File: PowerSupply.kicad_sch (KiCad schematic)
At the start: 0 parts

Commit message: i have added a few resistores
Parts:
- added C1: CL10A475KO8NNNC, easyeda2kicad:C0603, symbol easyeda2kicad:CL10A475KO8NNNC
- added R1: 0603WAF1003T5E, easyeda2kicad:R0603, symbol easyeda2kicad:0603WAF1003T5E
- added U1: TPS55288RPMR, easyeda2kicad:VQFN-HR-26_L4.0-W3.5_TPS55288RPMR, symbol easyeda2kicad:TPS55288RPMR
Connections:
- new net: C1.1, U1.19 (VCC)
- new net GND: C1.2

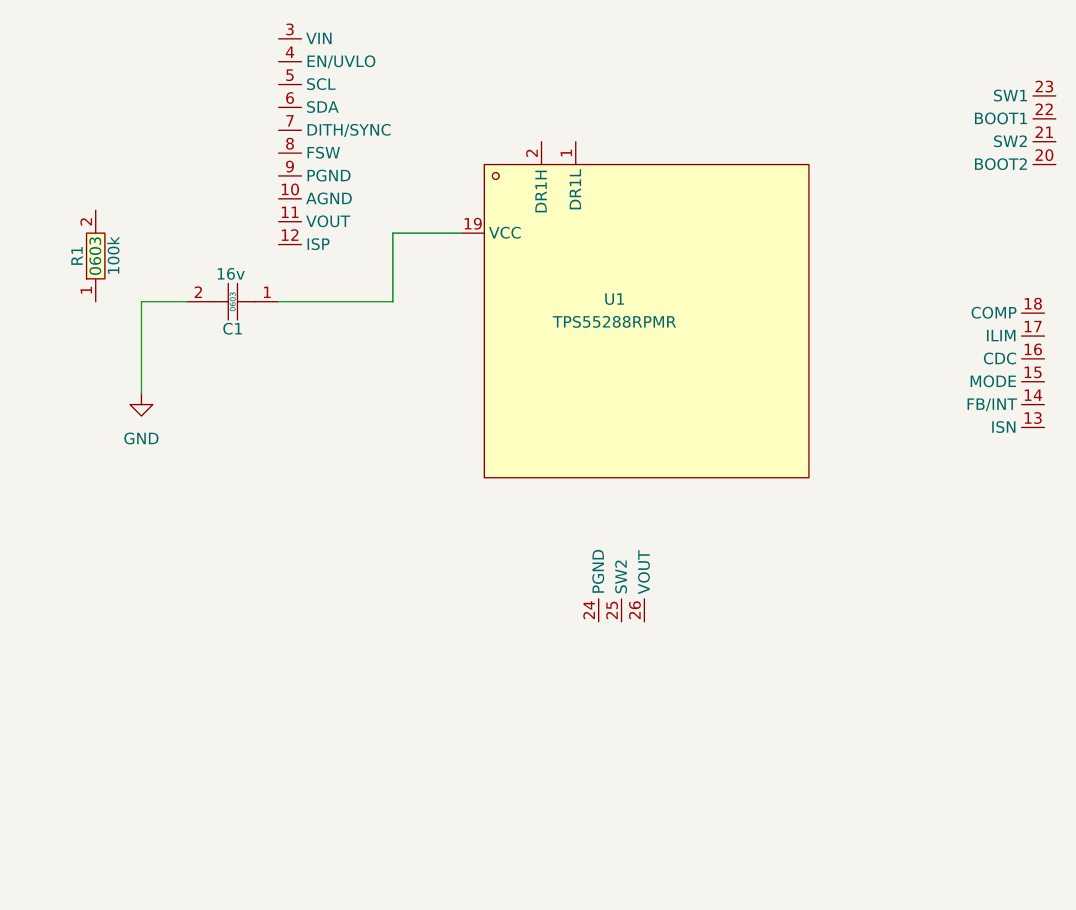
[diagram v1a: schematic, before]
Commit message: Added a few cap + res+ transistors
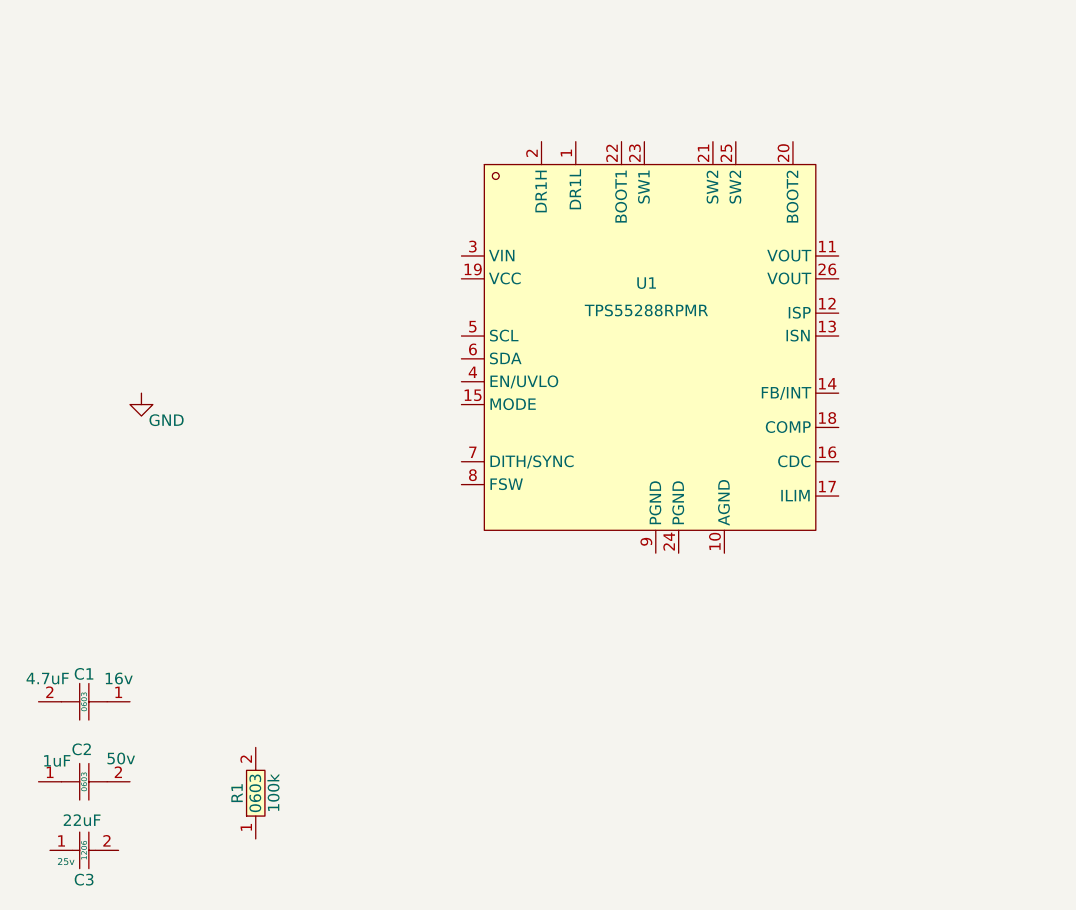
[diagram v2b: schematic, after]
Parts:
- added C2: CL10A105KB8NNNC, easyeda2kicad:C0603, symbol easyeda2kicad:CL10A105KB8NNNC
- added C3: CL31A226KAHNNNE, easyeda2kicad:C1206, symbol easyeda2kicad:CL31A226KAHNNNE
- C1: Field8 (none) -> 4.7uF
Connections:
- net GND: no longer C1.2
- net at C1.1: no longer U1.19 (VCC)
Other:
- moved on the sheet: C1, R1, U1

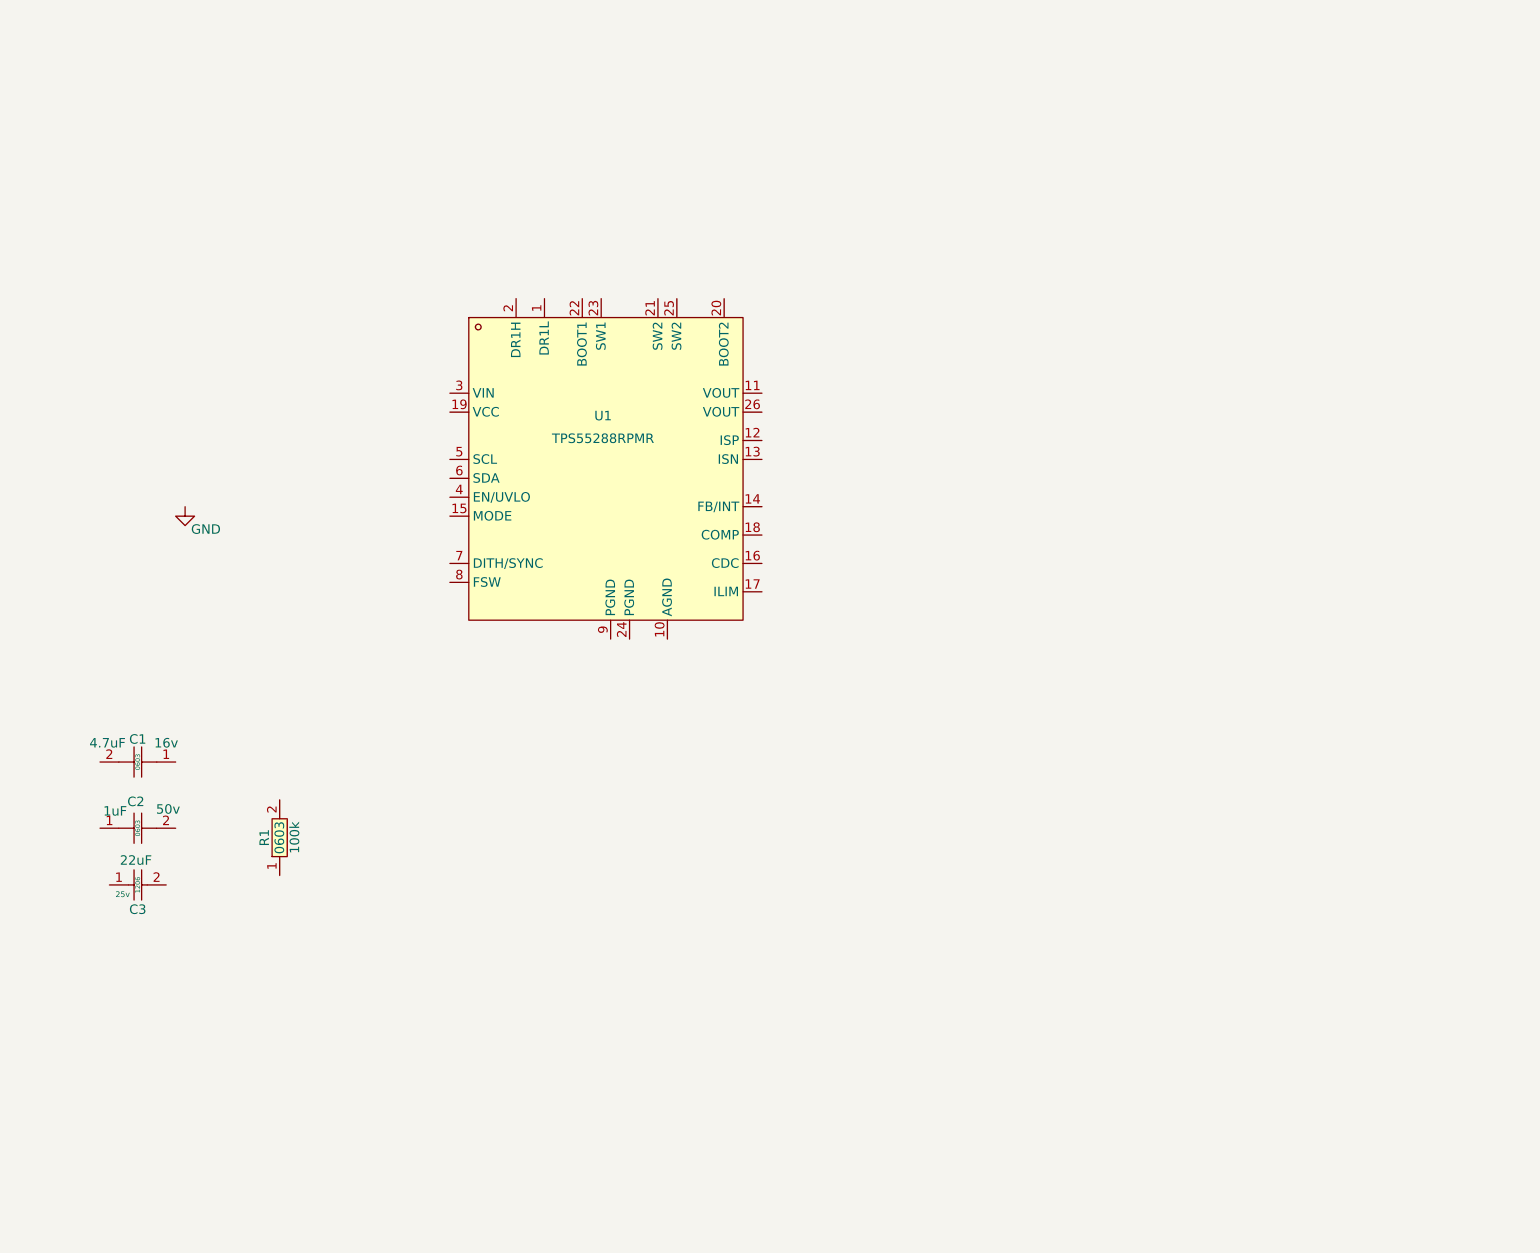
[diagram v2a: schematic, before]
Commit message: Recreate TPS block in KiCad with 0603+ components
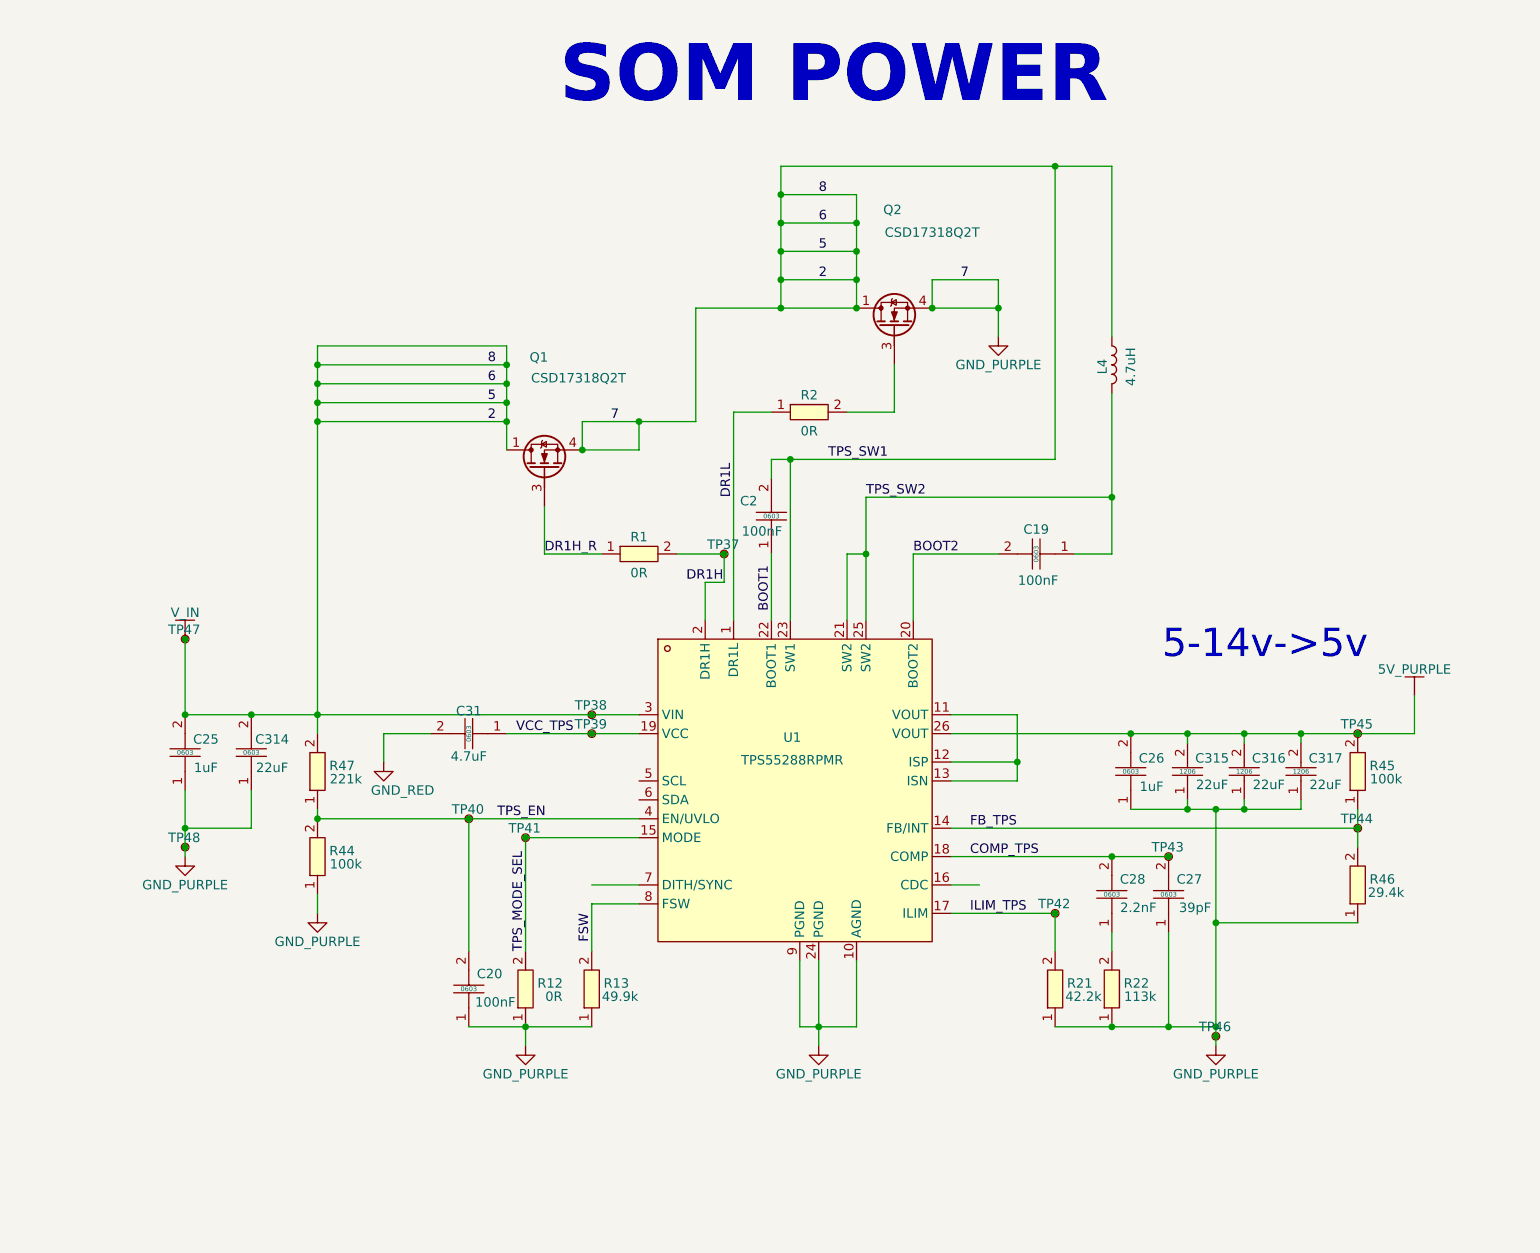
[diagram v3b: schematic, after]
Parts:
- removed C2: CL10A105KB8NNNC, easyeda2kicad:C0603, symbol easyeda2kicad:CL10A105KB8NNNC
- removed C3: CL31A226KAHNNNE, easyeda2kicad:C1206, symbol easyeda2kicad:CL31A226KAHNNNE
- added C19, C2, C20: CC0603KRX7R9BB104, easyeda2kicad:C0603, symbol easyeda2kicad:CL10A475KO8NNNC
- added C25, C26: CL10A105KB8NNNC, easyeda2kicad:C0603, symbol easyeda2kicad:CL10A105KB8NNNC
- added C27: CC0603JRNPO9BN390, easyeda2kicad:C0603, symbol easyeda2kicad:CL10A475KO8NNNC
- added C28: CL10B222KB8NNNC, easyeda2kicad:C0603, symbol easyeda2kicad:CL10A475KO8NNNC
- added C314: CL10A226MO7JZNC, easyeda2kicad:C0603, symbol easyeda2kicad:CL10A105KB8NNNC
- added C315, C316, C317: CL31A226KAHNNNE, easyeda2kicad:C1206, symbol easyeda2kicad:CL31A226KAHNNNE
- added L4: LQM18PN4R7MFRL, 2020, symbol Device:L
- added Q1, Q2: CSD17318Q2T, Package_TO_SOT_SMD:TDSON-8-1, symbol Transistor_FET:CSD17310Q5A
- added R1, R12, R2: RC0603JR-070RL, easyeda2kicad:R0603, symbol easyeda2kicad:0603WAF1003T5E
- added R13: RC0603FR-0749K9L, easyeda2kicad:R0603, symbol easyeda2kicad:0603WAF1003T5E
- added R21: CRCW060342K2FKEA, easyeda2kicad:R0603, symbol easyeda2kicad:0603WAF1003T5E
- added R22: PTFR0603B113KP9, easyeda2kicad:R0603, symbol easyeda2kicad:0603WAF1003T5E
- added R44: 0603WAF1003T5E, easyeda2kicad:R0603, symbol easyeda2kicad:0603WAF1003T5E
- added R46: FRC0603F2942TS, easyeda2kicad:R0603, symbol easyeda2kicad:0603WAF1003T5E
- added R47: FRC0603F2213TS, easyeda2kicad:R0603, symbol easyeda2kicad:0603WAF1003T5E
- added TP37, TP38, TP39, TP40, TP41, TP42, TP43, TP44, TP45, TP46, TP47, TP48: TestPoint_Small, symbol Connector:TestPoint_Small
- renumbered C1 to C31, R1 to R45
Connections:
- net VCC_TPS: now reaches C31.1
- net VCC_TPS: now also U1.19 (VCC), TP39.1
- net GND_RED: now reaches C31.2
- net FB_TPS: now reaches R45.1
- net FB_TPS: now also U1.14 (FB/INT), R46.2, TP44.1
- net +5V: now reaches R45.2
- net +5V: now also U1.10 (AGND), U1.23 (SW1), U1.24 (PGND), U1.26 (VOUT), U1.3 (VIN), U1.9 (PGND), C2.2, C20.1, C25.1, C25.2, C26.1, C26.2, C27.1, C314.1, C314.2, C315.1, C315.2, C316.1, C316.2, C317.1, C317.2, L4.1, Q1.1 (D), Q1.2 (S), Q1.3 (S), Q1.4 (S), Q2.1 (D), Q2.2 (S), Q2.3 (S), Q2.4 (S), R12.1, R13.1, R21.1, R22.1, R44.1, R46.1, R47.2, TP38.1, TP45.1, TP46.1, TP47.1, TP48.1
- net DR1L: now reaches U1.1 (DR1L)
- net DR1L: now also R2.1
- net at U1.11 (VOUT): now also U1.12 (ISP), U1.13 (ISN)
- net TPS_MODE_SEL: now reaches U1.15 (MODE)
- net TPS_MODE_SEL: now also R12.2, TP41.1
- net ILIM_TPS: now reaches U1.17 (ILIM)
- net ILIM_TPS: now also R21.2, TP42.1
- net COMP_TPS: now reaches U1.18 (COMP)
- net COMP_TPS: now also C27.2, C28.2, TP43.1
- net at U1.2 (DR1H): now also R1.2, TP37.1
- net BOOT2: now reaches U1.20 (BOOT2)
- net BOOT2: now also C19.2
- net TPS_SW2: now reaches U1.21 (SW2)
- net TPS_SW2: now also U1.25 (SW2), C19.1, L4.2
- net BOOT1: now reaches U1.22 (BOOT1)
- net BOOT1: now also C2.1
- net TPS_EN: now reaches U1.4 (EN/UVLO)
- net TPS_EN: now also C20.2, R44.2, R47.1, TP40.1
- net FSW: now reaches U1.8 (FSW)
- net FSW: now also R13.2
- new net: Q2.3 (S), R2.2
- new net: C28.1, R22.2
- new net DR1H_R: Q1.3 (S), R1.1
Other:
- note added: "5-14v->5v"
- note added: "SOM POWER"
- moved on the sheet: C31, R45, U1

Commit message: Recreate TPS block in KiCad with 0603+ components
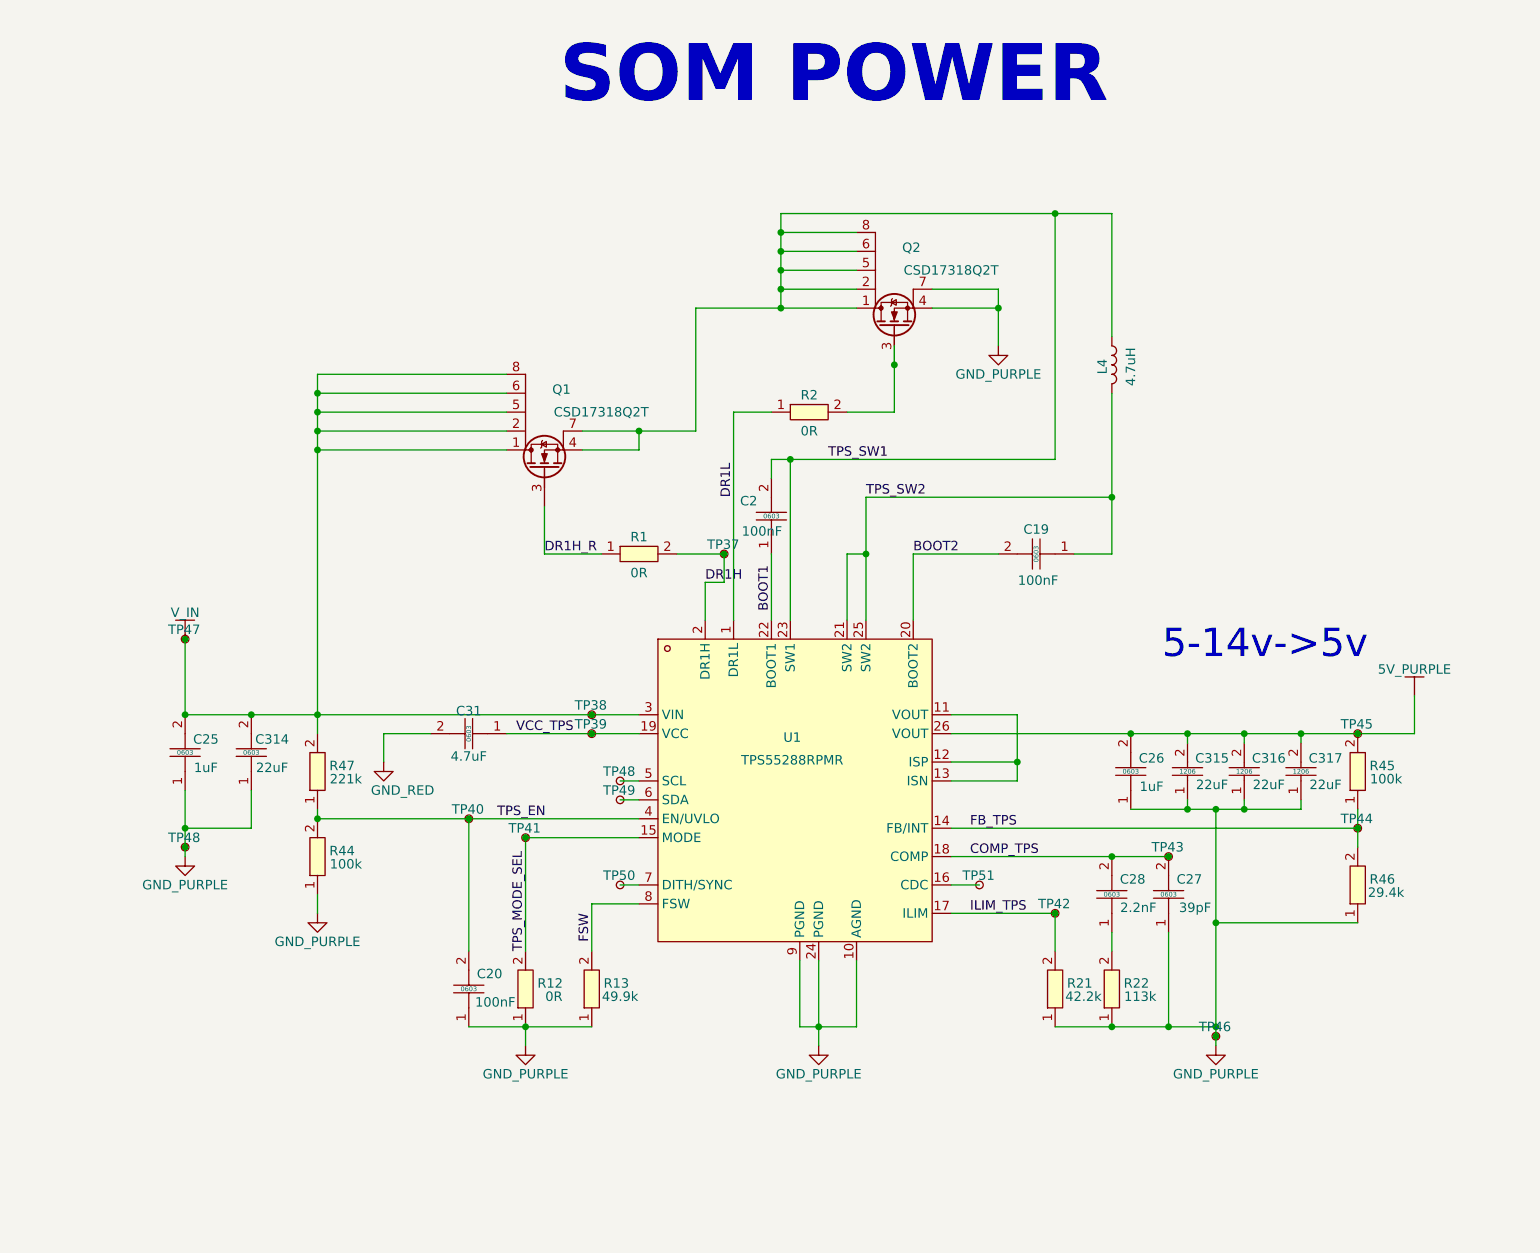
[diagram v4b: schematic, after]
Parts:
- added TP48, TP49, TP50, TP51: TestPoint_Small, symbol Connector:TestPoint_Small
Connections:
- net +5V: now also Q1.5 (D), Q1.6 (D), Q1.8 (D); no longer C2.2, C20.1, C25.1, C26.1, C27.1, C314.1, C315.1, C316.1, C317.1, L4.1, Q1.3 (S), Q1.4 (S), Q2.1 (D), Q2.2 (S), Q2.3 (S), Q2.4 (S), R12.1, R13.1, R21.1, R22.1, R44.1, R46.1, TP46.1, TP48.1, U1.10 (AGND), U1.23 (SW1), U1.24 (PGND), U1.9 (PGND)
- net DR1H: now also R1.2, TP37.1, U1.2 (DR1H)
- net at U1.16 (CDC): now also TP51.1
- net at U1.5 (SCL): now also TP48.1
- net at U1.6 (SDA): now also TP49.1
- net at U1.7 (DITH/SYNC): now also TP50.1
- new net GND_PURPLE: C20.1, C25.1, C26.1, C27.1, C314.1, C315.1, C316.1, C317.1, Q2.2 (S), Q2.3 (S), Q2.4 (S), Q2.7 (D), R12.1, R13.1, R21.1, R22.1, R44.1, R46.1, TP46.1, TP48.1, U1.10 (AGND), U1.24 (PGND), U1.9 (PGND)
- new net TPS_SW1: C2.2, L4.1, Q1.2 (S), Q1.3 (S), Q1.4 (S), Q1.7 (D), Q2.1 (D), Q2.2 (S), Q2.5 (D), Q2.6 (D), Q2.8 (D), U1.23 (SW1)
